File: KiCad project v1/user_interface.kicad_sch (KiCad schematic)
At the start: 12 parts, among them J4 Conn_01x05, J6 B4B-XH-AM__LF__SN_, Q2 BC817, Q3 BC817, SW1 SMD_6x3.5mm_h2.5mm, SW2 SMD_6x3.5mm_h2.5mm

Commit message: Completed symbol and footprint associations.
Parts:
- R13, R36, R37, R38: footprint (none) -> Resistor_SMD:R_0201_0603Metric
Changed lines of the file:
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@@
 			)
 		)
-		(property "Footprint" ""
+		(property "Footprint" "Resistor_SMD:R_0201_0603Metric"
 			(at 197.358 59.69 90)
 			(effects
@@
 			)
 		)
-		(property "Footprint" ""
+		(property "Footprint" "Resistor_SMD:R_0201_0603Metric"
 			(at 162.56 126.492 90)
 			(effects
@@
 			)
 		)
-		(property "Footprint" ""
+		(property "Footprint" "Resistor_SMD:R_0201_0603Metric"
 			(at 146.558 58.42 90)
 			(effects
@@
 			)
 		)
-		(property "Footprint" ""
+		(property "Footprint" "Resistor_SMD:R_0201_0603Metric"
 			(at 162.56 113.538 90)
 			(effects

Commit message: Small fixes.
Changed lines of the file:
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@@
 	(paper "A4")
+	(junction
+		(at 154.94 128.27)
+		(diameter 0)
+		(color 0 0 0 0)
+	)
 	(junction
 		(at 195.58 69.85)
@@
 	)
 	(junction
-		(at 155.575 128.27)
-		(diameter 0)
-		(color 0 0 0 0)
-	)
-	(junction
-		(at 156.21 111.76)
+		(at 157.48 111.76)
 		(diameter 0)
 		(color 0 0 0 0)
@@
 	(wire
 		(pts
-			(xy 156.21 111.76) (xy 158.75 111.76)
-		)
-		(stroke
-			(width 0)
-			(type default)
-		)
-	)
-	(wire
-		(pts
 			(xy 144.78 62.23) (xy 144.78 68.58)
 		)
@@
 	(wire
 		(pts
+			(xy 157.48 111.76) (xy 158.75 111.76)
+		)
+		(stroke
+			(width 0)
+			(type default)
+		)
+	)
+	(wire
+		(pts
 			(xy 154.94 85.09) (xy 154.94 87.63)
 		)
@@
 	(wire
 		(pts
-			(xy 156.21 111.76) (xy 156.21 120.65)
+			(xy 157.48 111.76) (xy 157.48 121.92)
 		)
 		(stroke
@@
 	(wire
 		(pts
-			(xy 181.61 123.19) (xy 181.61 120.65)
+			(xy 154.94 128.27) (xy 158.75 128.27)
+		)
+		(stroke
+			(width 0)
+			(type default)
+		)
+	)
+	(wire
+		(pts
+			(xy 181.61 123.19) (xy 181.61 121.92)
 		)
 		(stroke
@@
 	(wire
 		(pts
-			(xy 155.575 119.38) (xy 155.575 128.27)
-		)
-		(stroke
-			(width 0)
-			(type default)
-		)
-	)
-	(wire
-		(pts
-			(xy 181.61 119.38) (xy 155.575 119.38)
-		)
-		(stroke
-			(width 0)
-			(type default)
-		)
-	)
-	(wire
-		(pts
-			(xy 181.61 120.65) (xy 156.21 120.65)
-		)
-		(stroke
-			(width 0)
-			(type default)
-		)
-	)
-	(wire
-		(pts
-			(xy 149.86 128.27) (xy 155.575 128.27)
+			(xy 154.94 119.38) (xy 154.94 128.27)
+		)
+		(stroke
+			(width 0)
+			(type default)
+		)
+	)
+	(wire
+		(pts
+			(xy 181.61 119.38) (xy 154.94 119.38)
+		)
+		(stroke
+			(width 0)
+			(type default)
+		)
+	)
+	(wire
+		(pts
+			(xy 181.61 121.92) (xy 157.48 121.92)
+		)
+		(stroke
+			(width 0)
+			(type default)
+		)
+	)
+	(wire
+		(pts
+			(xy 149.86 128.27) (xy 154.94 128.27)
 		)
 		(stroke
@@
 	(wire
 		(pts
-			(xy 155.575 128.27) (xy 158.75 128.27)
-		)
-		(stroke
-			(width 0)
-			(type default)
-		)
-	)
-	(wire
-		(pts
 			(xy 195.58 63.5) (xy 195.58 69.85)
 		)
@@
 	(wire
 		(pts
-			(xy 149.86 111.76) (xy 156.21 111.76)
+			(xy 149.86 111.76) (xy 157.48 111.76)
 		)
 		(stroke
@@
 		)
 	)
+	(text_box "To learn more about the boot mode selection,\nsee documentation at https://txplo.re/esp32boot"
+		(exclude_from_sim no)
+		(at 198.755 131.445 0)
+		(size 29.845 11.43)
+		(stroke
+			(width 0)
+			(type default)
+		)
+		(fill
+			(type none)
+		)
+		(effects
+			(font
+				(size 1.27 1.27)
+			)
+			(justify left top)
+		)
+	)

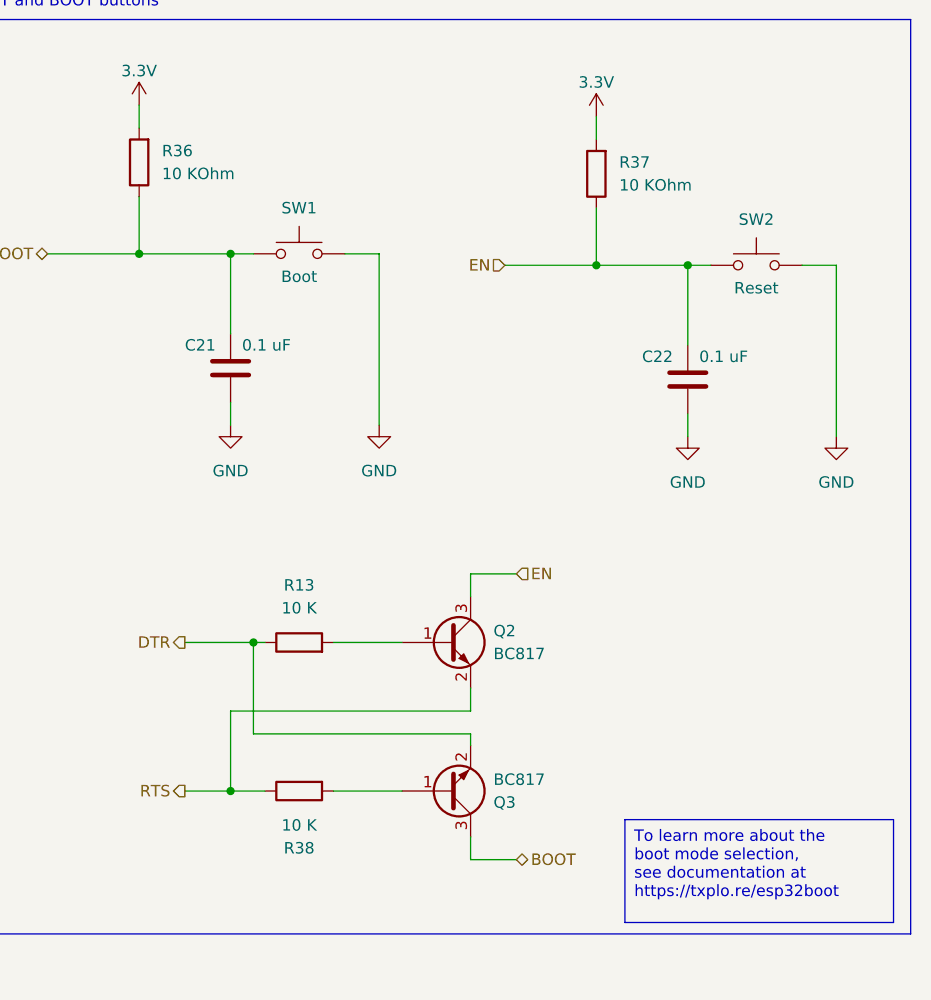
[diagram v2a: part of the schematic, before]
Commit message: Simplifying component values by removing units.
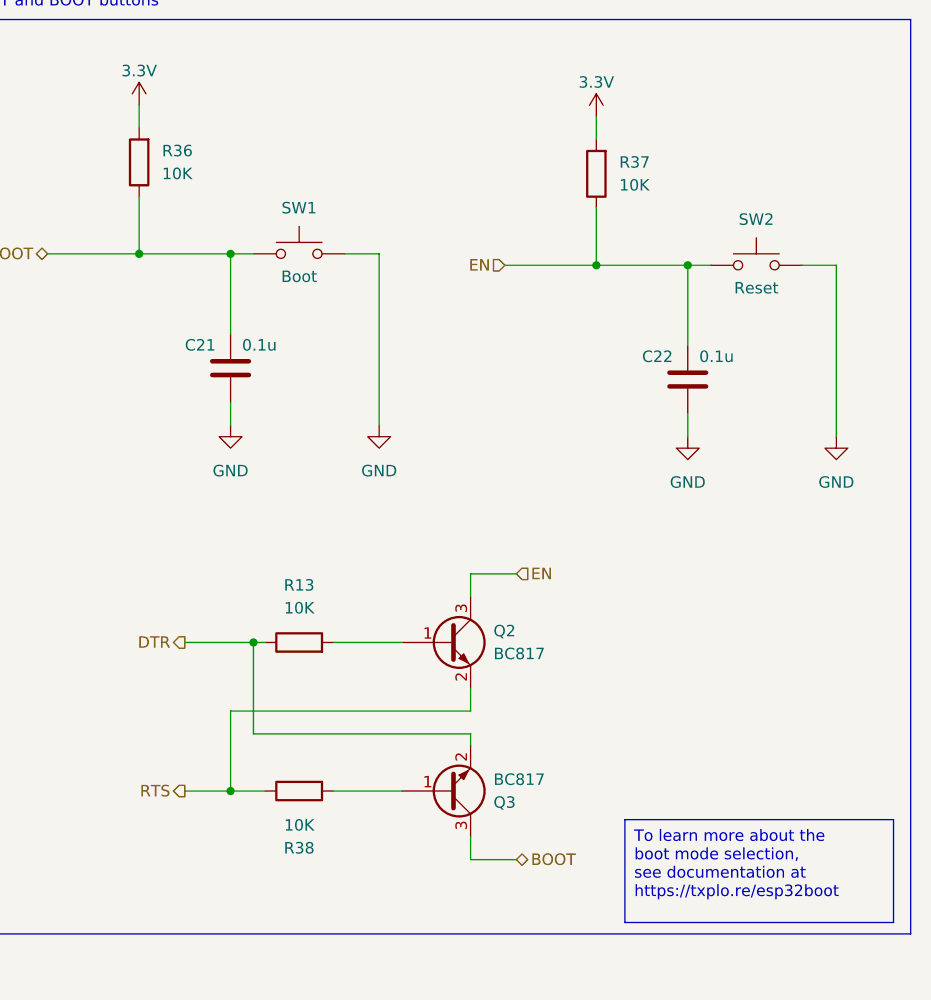
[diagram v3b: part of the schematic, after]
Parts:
- C21, C22: value 0.1 uF -> 0.1u
- R13, R38: value 10 K -> 10K
- R36, R37: value 10 KOhm -> 10K
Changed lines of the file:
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@@
 			)
 		)
-		(property "Value" "0.1 uF"
+		(property "Value" "0.1u"
 			(at 207.01 80.01 0)
 			(effects
@@
 			)
 		)
-		(property "Value" "0.1 uF"
+		(property "Value" "0.1u"
 			(at 156.21 78.74 0)
 			(effects
@@
 			)
 		)
-		(property "Value" "10 KOhm"
+		(property "Value" "10K"
 			(at 198.12 60.9599 0)
 			(effects
@@
 			)
 		)
-		(property "Value" "10 K"
+		(property "Value" "10K"
 			(at 162.56 132.08 90)
 			(effects
@@
 			)
 		)
-		(property "Value" "10 KOhm"
+		(property "Value" "10K"
 			(at 147.32 59.6899 0)
 			(effects
@@
 			)
 		)
-		(property "Value" "10 K"
+		(property "Value" "10K"
 			(at 162.56 107.95 90)
 			(effects
